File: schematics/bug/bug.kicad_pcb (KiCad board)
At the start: 2 copper layers, 16 parts, among them P1 CONN_01X09, P2 CONN_01X02, P3 CONN_01X06, P4 CONN_01X02, U1 uln2803A, U2 Arduino_Mini, U3 SPX2920U-3.3, U4 ESP8266, U5 button

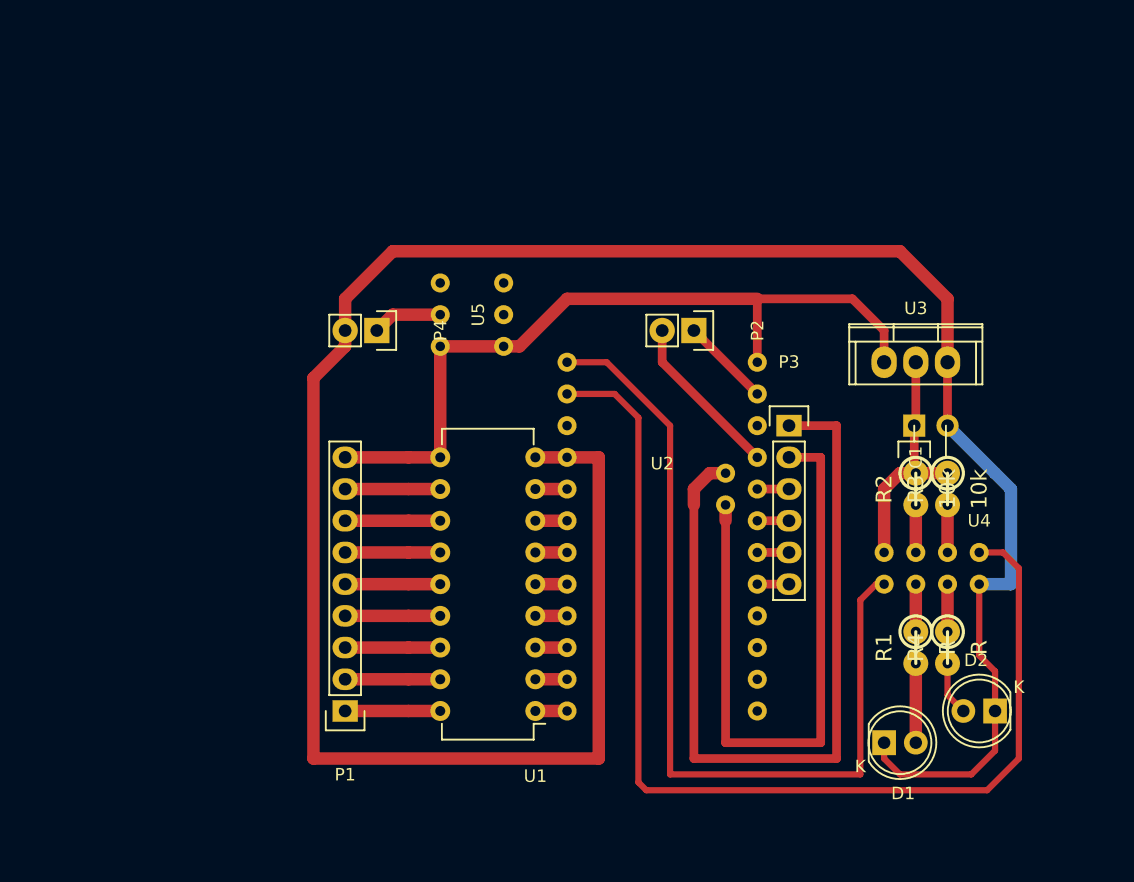
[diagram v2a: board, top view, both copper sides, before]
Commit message: SCHEMATIC: move button and led to one place
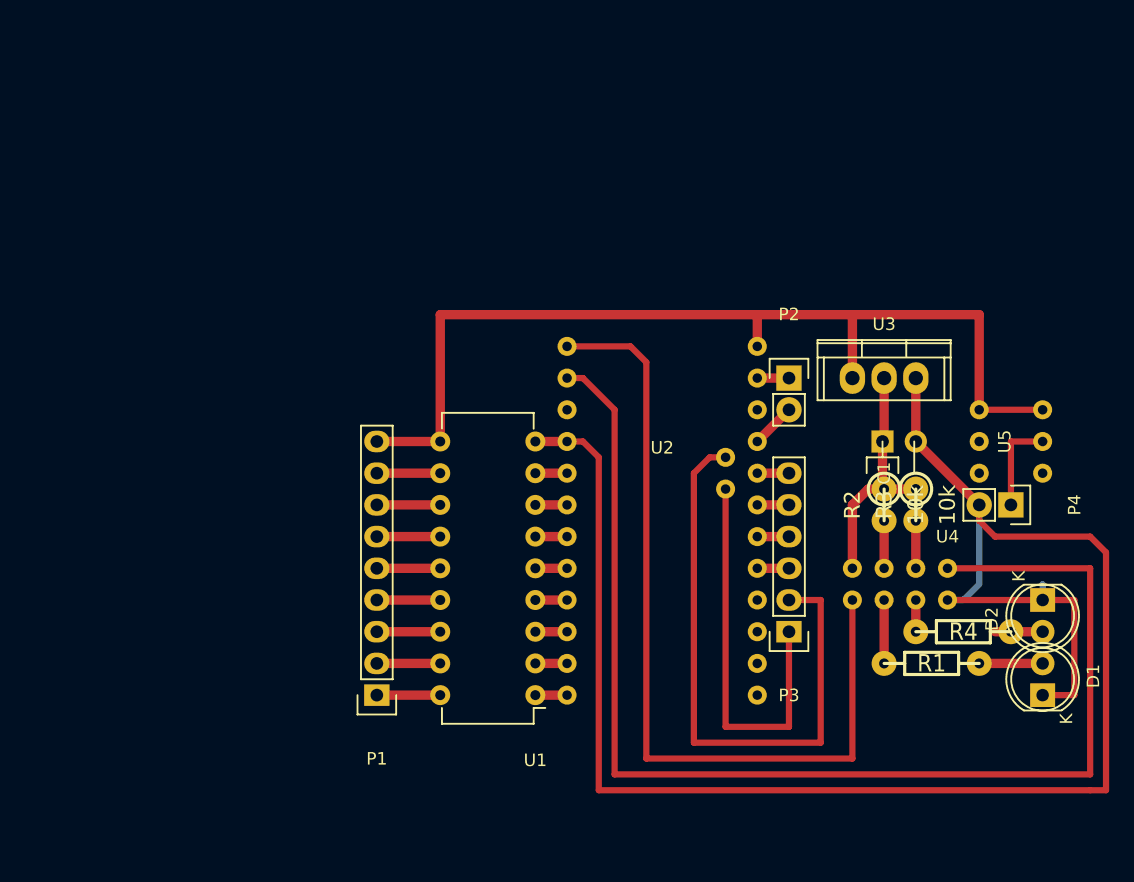
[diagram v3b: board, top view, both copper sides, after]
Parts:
- R1, R4: footprint w_pth_resistors:rc05_vert -> w_pth_resistors:RC03
- moved P4 52.7 mm to (172.7, 111.8)
- moved U5 44.4 mm to (172.7, 106.7), turned to 270 degrees
- moved P3 16.5 mm to (154.9, 121.9), turned to 180 degrees
- moved D1 13.3 mm to (175.3, 127.0), turned to 90 degrees
- moved D2 9.67 mm to (175.3, 119.4), turned to 270 degrees
- moved P2 8.52 mm to (154.9, 101.6), turned to 0 degrees
- moved P1 2.84 mm to (121.9, 127.0)
- moved C1 2.84 mm to (165.1, 106.7)
- moved R2 2.84 mm to (162.6, 111.8)
- moved R3 2.84 mm to (165.1, 111.8)
- moved R1 2.84 mm to (167.6, 124.5), turned to 0 degrees
- moved U3 2.84 mm to (162.6, 101.6)
- moved U4 2.84 mm to (165.1, 119.4)
- moved U1 1.27 mm to (134.6, 127.0)
- moved R4 1.27 mm to (167.6, 121.9), turned to 0 degrees
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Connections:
- U2 pad 11: Net-(P3-Pad3) -> Net-(P3-Pad6)
- U2 pad 12: Net-(P3-Pad4) -> Net-(P3-Pad5)
- U2 pad 13: Net-(P3-Pad5) -> Net-(P3-Pad4)
- U2 pad 14: Net-(P3-Pad6) -> Net-(P3-Pad3)
- U2 pad 22: Net-(P3-Pad1) -> Net-(P3-Pad2)
- U2 pad 23: Net-(P3-Pad2) -> Net-(P3-Pad1)
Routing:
- net Net-(C1-Pad2): track 194.2 -> 148.3 mm
- net Net-(P3-Pad1): track 66.6 -> 31.7 mm
- net Net-(P1-Pad9): track 62.3 -> 78.7 mm
- net Net-(U2-Pad34): track 86.5 -> 100.1 mm
- net Net-(P2-Pad2): track 13.3 -> 3.59 mm
- net Net-(P2-Pad1): track 7.18 -> 2.54 mm
- net Net-(P3-Pad2): track 52.1 -> 48.8 mm
- net Net-(P1-Pad8): track 7.62 -> 5.08 mm
- net Net-(P1-Pad7): track 7.62 -> 5.08 mm
- net Net-(P1-Pad6): track 7.62 -> 5.08 mm
- net Net-(P1-Pad5): track 7.62 -> 5.08 mm
- net Net-(P1-Pad4): track 7.62 -> 5.08 mm
- net Net-(P1-Pad3): track 7.62 -> 5.08 mm
- net Net-(P1-Pad2): track 7.62 -> 5.08 mm
- net Net-(P1-Pad1): track 7.62 -> 5.08 mm
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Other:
- net class Default: trace_width 0.25 -> 0.75

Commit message: SCHEMATIC: update lineSensors and bug
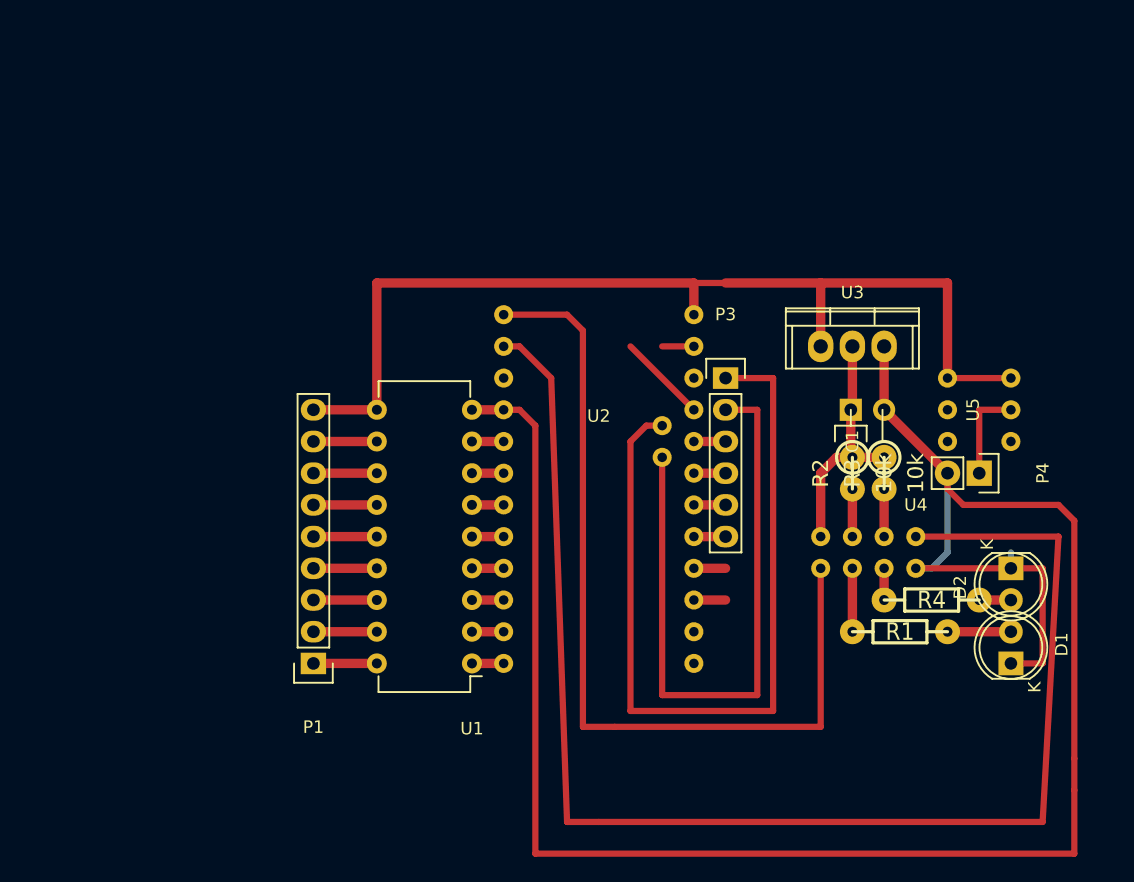
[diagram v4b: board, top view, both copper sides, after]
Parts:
- removed P2: CONN_01X02, Pin_Headers:Pin_Header_Straight_1x02
- moved P3 20.9 mm to (149.9, 101.6), turned to 0 degrees
- moved U1 5.68 mm to (129.5, 124.5)
- moved U2 5.68 mm to (139.7, 104.1)
- moved P1 5.68 mm to (116.8, 124.5)
- moved C1 3.59 mm to (162.6, 104.1)
- moved D1 3.59 mm to (172.7, 124.5)
- moved P4 3.59 mm to (170.2, 109.2)
- moved R2 3.59 mm to (160.0, 109.2)
- moved R3 3.59 mm to (162.6, 109.2)
- moved R4 3.59 mm to (165.1, 119.4)
- moved U5 3.59 mm to (170.2, 104.1)
- moved D2 3.59 mm to (172.7, 116.8)
- moved R1 3.59 mm to (165.1, 121.9)
- moved U3 3.59 mm to (160.0, 99.1)
- moved U4 3.59 mm to (162.6, 116.8)
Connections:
- U2 pad 11: Net-(P3-Pad6) -> Net-(P3-Pad3)
- U2 pad 12: Net-(P3-Pad5) -> Net-(P3-Pad4)
- U2 pad 13: Net-(P3-Pad4) -> Net-(P3-Pad5)
- U2 pad 14: Net-(P3-Pad3) -> Net-(P3-Pad6)
- U2 pad 22: Net-(P3-Pad2) -> Net-(P3-Pad1)
- U2 pad 23: Net-(P3-Pad1) -> Net-(P3-Pad2)
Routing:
- net Net-(P3-Pad1): track 31.7 -> 66.6 mm
- net Net-(C1-Pad2): track 148.3 -> 166.0 mm
- net Net-(U2-Pad34): track 100.1 -> 112.9 mm
- net Net-(U2-Pad10): track 3.59 -> 7.18 mm
- net Net-(P3-Pad2): track 48.8 -> 52.1 mm
- net Net-(U2-Pad16): track 0.00 -> 2.54 mm
- net Net-(U2-Pad15): track 0.00 -> 2.54 mm
- net Net-(P1-Pad9): track 78.7 -> 81.3 mm
- net Net-(U2-Pad35): track 67.8 -> 70.4 mm
- net Net-(D2-Pad2): track 3.81 -> 2.54 mm

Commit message: Cleanup repository
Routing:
- net Net-(C1-Pad2): track 166.0 -> 150.8 mm
- net Net-(U2-Pad34): track 112.9 -> 102.7 mm
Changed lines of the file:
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@@
     (links 47)
     (no_connects 0)
-    (area 106.579999 37.999999 182.980001 137.260001)
+    (area 106.579999 37.999999 182.980001 140.150002)
     (thickness 1.6)
     (drawings 10)
-    (tracks 104)
+    (tracks 103)
     (zones 0)
     (modules 15)
@@
   (segment (start 157.48 109.22) (end 158.75 107.95) (width 0.75) (layer F.Cu) (net 1))
   (segment (start 157.48 114.3) (end 157.48 109.22) (width 0.75) (layer F.Cu) (net 1))
-  (segment (start 134.62 139.7) (end 177.8 139.7) (width 0.5) (layer F.Cu) (net 2))
+  (segment (start 134.62 132.08) (end 177.8 132.08) (width 0.5) (layer F.Cu) (net 2))
   (segment (start 167.64 110.49) (end 168.91 111.76) (width 0.5) (layer F.Cu) (net 2))
   (segment (start 168.91 111.76) (end 176.53 111.76) (width 0.5) (layer F.Cu) (net 2))
   (segment (start 176.53 111.76) (end 177.8 113.03) (width 0.5) (layer F.Cu) (net 2))
   (segment (start 177.8 113.03) (end 177.8 132.08) (width 0.5) (layer F.Cu) (net 2))
-  (segment (start 177.8 132.08) (end 177.8 134.62) (width 0.5) (layer F.Cu) (net 2))
-  (segment (start 177.8 134.62) (end 177.8 139.7) (width 0.5) (layer F.Cu) (net 2))
-  (segment (start 134.62 139.7) (end 134.62 105.41) (width 0.5) (layer F.Cu) (net 2))
+  (segment (start 177.8 132.08) (end 177.8 132.08) (width 0.5) (layer F.Cu) (net 2))
+  (segment (start 177.8 132.08) (end 177.8 132.08) (width 0.5) (layer F.Cu) (net 2))
+  (segment (start 134.62 132.08) (end 134.62 105.41) (width 0.5) (layer F.Cu) (net 2))
   (segment (start 134.62 105.41) (end 133.35 104.14) (width 0.5) (layer F.Cu) (net 2))
   (segment (start 132.08 104.14) (end 133.35 104.14) (width 0.5) (layer F.Cu) (net 2))
@@
   (segment (start 132.08 104.14) (end 129.54 104.14) (width 0.75) (layer F.Cu) (net 2))
   (segment (start 167.64 121.92) (end 172.72 121.92) (width 0.75) (layer F.Cu) (net 3))
-  (segment (start 172.72 119.38) (end 170.18 119.38) (width 0.75) (layer F.Cu) (net 4) (status C00000))
+  (segment (start 172.72 119.38) (end 170.18 119.38) (width 0.75) (layer F.Cu) (net 4))
   (segment (start 116.84 124.46) (end 121.92 124.46) (width 0.75) (layer F.Cu) (net 5))
   (segment (start 116.84 121.92) (end 121.92 121.92) (width 0.75) (layer F.Cu) (net 6))
@@
   (segment (start 121.92 109.22) (end 116.84 109.22) (width 0.75) (layer F.Cu) (net 11))
   (segment (start 116.84 106.68) (end 121.92 106.68) (width 0.75) (layer F.Cu) (net 12))
-  (segment (start 147.32 93.98) (end 149.86 93.98) (width 0.5) (layer F.Cu) (net 13))
-  (segment (start 149.86 93.98) (end 157.48 93.98) (width 0.75) (layer F.Cu) (net 13))
+  (segment (start 157.48 93.98) (end 147.32 93.98) (width 0.75) (layer F.Cu) (net 13))
   (segment (start 157.48 99.06) (end 157.48 93.98) (width 0.75) (layer F.Cu) (net 13))
   (segment (start 157.48 93.98) (end 167.64 93.98) (width 0.75) (layer F.Cu) (net 13))
@@
   (segment (start 147.32 96.52) (end 147.32 93.98) (width 0.75) (layer F.Cu) (net 13))
   (segment (start 121.92 93.98) (end 121.92 104.14) (width 0.75) (layer F.Cu) (net 13))
+  (segment (start 147.32 93.98) (end 121.92 93.98) (width 0.75) (layer F.Cu) (net 13))
   (segment (start 116.84 104.14) (end 121.92 104.14) (width 0.75) (layer F.Cu) (net 13))
-  (segment (start 147.32 93.98) (end 121.92 93.98) (width 0.75) (layer F.Cu) (net 13))
   (segment (start 142.24 128.27) (end 153.67 128.27) (width 0.5) (layer F.Cu) (net 14))
   (segment (start 144.78 105.41) (end 143.51 105.41) (width 0.5) (layer F.Cu) (net 14))
@@
   (segment (start 147.32 116.84) (end 149.86 116.84) (width 0.75) (layer F.Cu) (net 33))
   (segment (start 149.86 116.84) (end 149.86 116.84) (width 2) (layer F.Cu) (net 33))
-  (segment (start 139.7 137.16) (end 137.16 137.16) (width 0.5) (layer F.Cu) (net 34))
+  (segment (start 139.7 130.81) (end 135.89 130.81) (width 0.5) (layer F.Cu) (net 34))
   (segment (start 133.35 99.06) (end 135.89 101.6) (width 0.5) (layer F.Cu) (net 34))
-  (segment (start 135.89 101.6) (end 137.16 137.16) (width 0.5) (layer F.Cu) (net 34))
-  (segment (start 139.7 137.16) (end 175.26 137.16) (width 0.5) (layer F.Cu) (net 34))
-  (segment (start 175.26 137.16) (end 176.53 114.3) (width 0.5) (layer F.Cu) (net 34))
+  (segment (start 135.89 101.6) (end 135.89 130.81) (width 0.5) (layer F.Cu) (net 34))
+  (segment (start 139.7 130.81) (end 176.53 130.81) (width 0.5) (layer F.Cu) (net 34))
+  (segment (start 176.53 130.81) (end 176.53 114.3) (width 0.5) (layer F.Cu) (net 34))
   (segment (start 165.1 114.3) (end 176.53 114.3) (width 0.5) (layer F.Cu) (net 34))
   (segment (start 133.35 99.06) (end 132.08 99.06) (width 0.5) (layer F.Cu) (net 34))
